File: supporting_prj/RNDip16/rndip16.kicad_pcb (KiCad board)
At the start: 2 copper layers, 24.4 x 21 mm, 27 parts, among them J1 Conn_01x16_Pin, J2 Conn_01x16_Pin

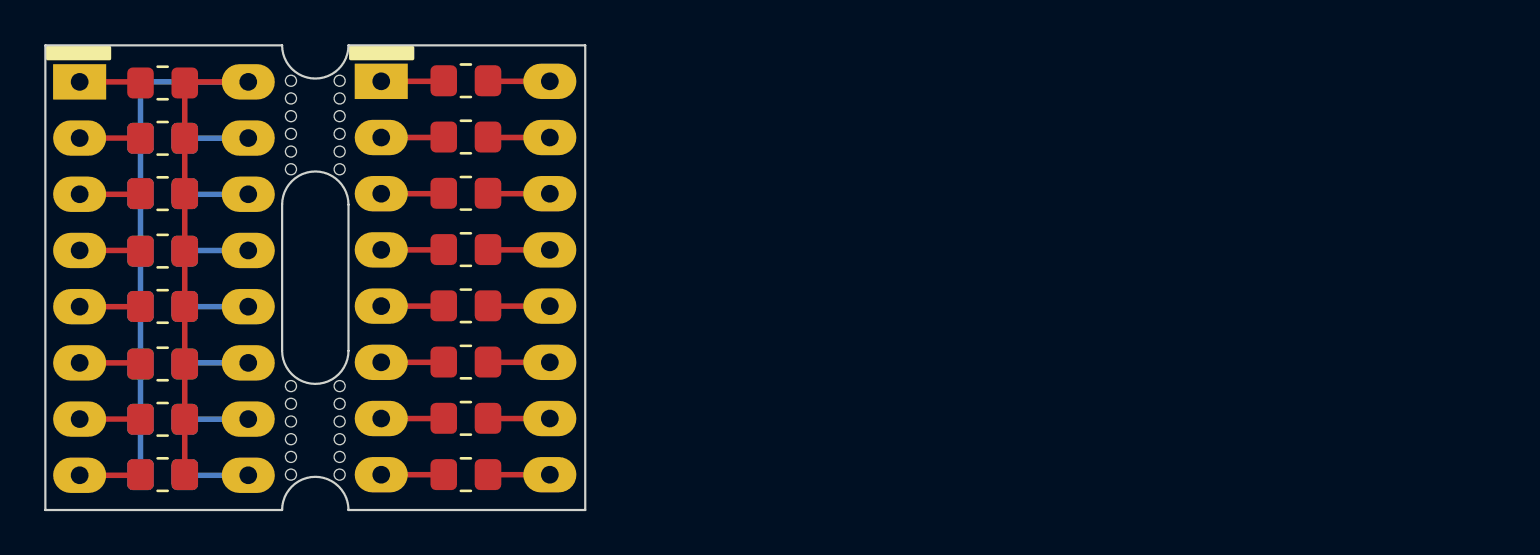
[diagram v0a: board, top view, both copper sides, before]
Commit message: RNDip fix
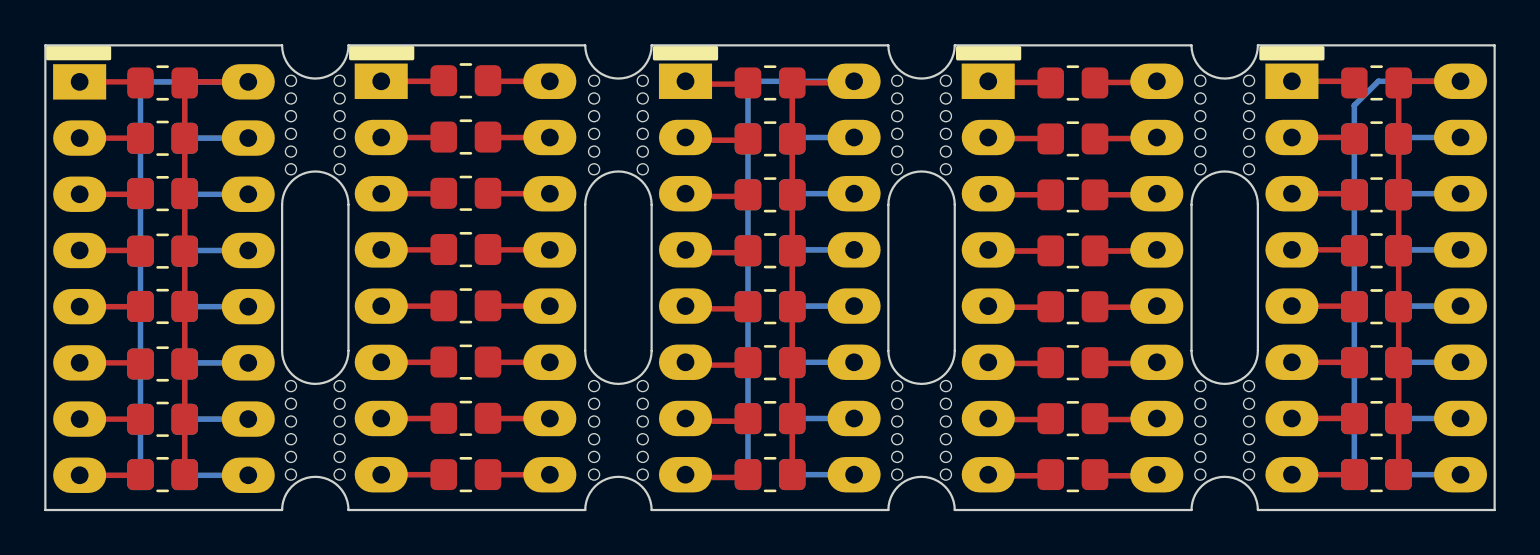
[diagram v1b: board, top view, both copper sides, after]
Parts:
- added J3: Conn_01x16_Pin, RNDip16:Dip16_package, F.Cu at (82.9, 47.5)
- added J4: Conn_01x16_Pin, RNDip16:Dip16_package, F.Cu at (96.6, 47.5)
- added J5: Conn_01x16_Pin, RNDip16:Dip16_package, F.Cu at (110.3, 47.5)
- added R24: R, RNDip16:R_0805, F.Cu at (86.8, 47.6)
- added R25: R, RNDip16:R_0805, F.Cu at (86.8, 50.1)
- added R26: R, RNDip16:R_0805, F.Cu at (86.8, 52.7)
- added R27: R, RNDip16:R_0805, F.Cu at (86.8, 55.2)
- added R28: R, RNDip16:R_0805, F.Cu at (86.8, 57.7)
- added R29: R, RNDip16:R_0805, F.Cu at (86.8, 60.2)
- added R30: R, RNDip16:R_0805, F.Cu at (86.8, 62.8)
- added R31: R, RNDip16:R_0805, F.Cu at (86.8, 65.3)
- added R32: R, RNDip16:R_0805, B.Cu at (86.8, 65.3)
- added R33: R, RNDip16:R_0805, B.Cu at (86.8, 62.8)
- added R34: R, RNDip16:R_0805, B.Cu at (86.8, 60.2)
- added R35: R, RNDip16:R_0805, B.Cu at (86.8, 57.7)
- added R36: R, RNDip16:R_0805, B.Cu at (86.8, 55.2)
- added R37: R, RNDip16:R_0805, B.Cu at (86.8, 52.7)
- added R38: R, RNDip16:R_0805, B.Cu at (86.8, 50.1)
- added R39: R, RNDip16:R_0805, F.Cu at (100.4, 47.6)
- added R40: R, RNDip16:R_0805, F.Cu at (100.4, 50.1)
- added R41: R, RNDip16:R_0805, F.Cu at (100.4, 52.7)
- added R42: R, RNDip16:R_0805, F.Cu at (100.4, 55.2)
- added R43: R, RNDip16:R_0805, F.Cu at (100.4, 57.7)
- added R44: R, RNDip16:R_0805, F.Cu at (100.4, 60.2)
- added R45: R, RNDip16:R_0805, F.Cu at (100.4, 62.8)
- added R46: R, RNDip16:R_0805, F.Cu at (100.4, 65.3)
- added R47: R, RNDip16:R_0805, F.Cu at (114.2, 47.6)
- added R48: R, RNDip16:R_0805, F.Cu at (114.2, 50.1)
- added R49: R, RNDip16:R_0805, F.Cu at (114.2, 52.7)
- added R50: R, RNDip16:R_0805, F.Cu at (114.2, 55.2)
- added R51: R, RNDip16:R_0805, F.Cu at (114.2, 57.7)
- added R52: R, RNDip16:R_0805, F.Cu at (114.2, 60.2)
- added R53: R, RNDip16:R_0805, F.Cu at (114.2, 62.8)
- added R54: R, RNDip16:R_0805, F.Cu at (114.2, 65.3)
- added R55: R, RNDip16:R_0805, B.Cu at (114.2, 65.3)
- added R56: R, RNDip16:R_0805, B.Cu at (114.2, 62.8)
- added R57: R, RNDip16:R_0805, B.Cu at (114.2, 60.2)
- added R58: R, RNDip16:R_0805, B.Cu at (114.2, 57.7)
- added R59: R, RNDip16:R_0805, B.Cu at (114.2, 55.2)
- added R60: R, RNDip16:R_0805, B.Cu at (114.2, 52.7)
- added R61: R, RNDip16:R_0805, B.Cu at (114.2, 50.1)
- added mouse-bite-2.54mm-slot_13: VAL**, RNDip16:mouse_bite, F.Cu at (107.3, 63.3)
- added mouse-bite-2.54mm-slot_13: VAL**, RNDip16:mouse_bite, F.Cu at (93.6, 49.5)
- added mouse-bite-2.54mm-slot_13: VAL**, RNDip16:mouse_bite, F.Cu at (79.9, 63.3)
- added mouse-bite-2.54mm-slot_13: VAL**, RNDip16:mouse_bite, F.Cu at (107.3, 49.5)
- added mouse-bite-2.54mm-slot_13: VAL**, RNDip16:mouse_bite, F.Cu at (93.6, 63.3)
- added mouse-bite-2.54mm-slot_13: VAL**, RNDip16:mouse_bite, F.Cu at (79.9, 49.5)
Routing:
- net Net-(J3-Pin_16): track 0.00 -> 42.9 mm
- net Net-(J5-Pin_16): track 0.00 -> 42.5 mm
- net Net-(J3-Pin_8): track 0.00 -> 2.88 mm
- net Net-(J3-Pin_7): track 0.00 -> 2.87 mm
- net Net-(J3-Pin_6): track 0.00 -> 2.87 mm
- net Net-(J3-Pin_5): track 0.00 -> 2.86 mm
- net Net-(J3-Pin_4): track 0.00 -> 2.86 mm
- net Net-(J5-Pin_1): track 0.00 -> 2.86 mm
- net Net-(J3-Pin_3): track 0.00 -> 2.86 mm
- net Net-(J5-Pin_2): track 0.00 -> 2.85 mm
- net Net-(J3-Pin_2): track 0.00 -> 2.85 mm
- net Net-(J4-Pin_8): track 0.00 -> 2.85 mm
- net Net-(J5-Pin_3): track 0.00 -> 2.85 mm
- net Net-(J3-Pin_1): track 0.00 -> 2.85 mm
- net Net-(J4-Pin_7): track 0.00 -> 2.84 mm
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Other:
- board size 24.4 x 21 mm -> 65.5 x 21 mm
- board text added: "15-in-1"
- board text added: "8-in-1"
